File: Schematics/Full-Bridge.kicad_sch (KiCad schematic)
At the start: 3 parts, among them J11 464379202, J12 43650-0418, J13 464369202

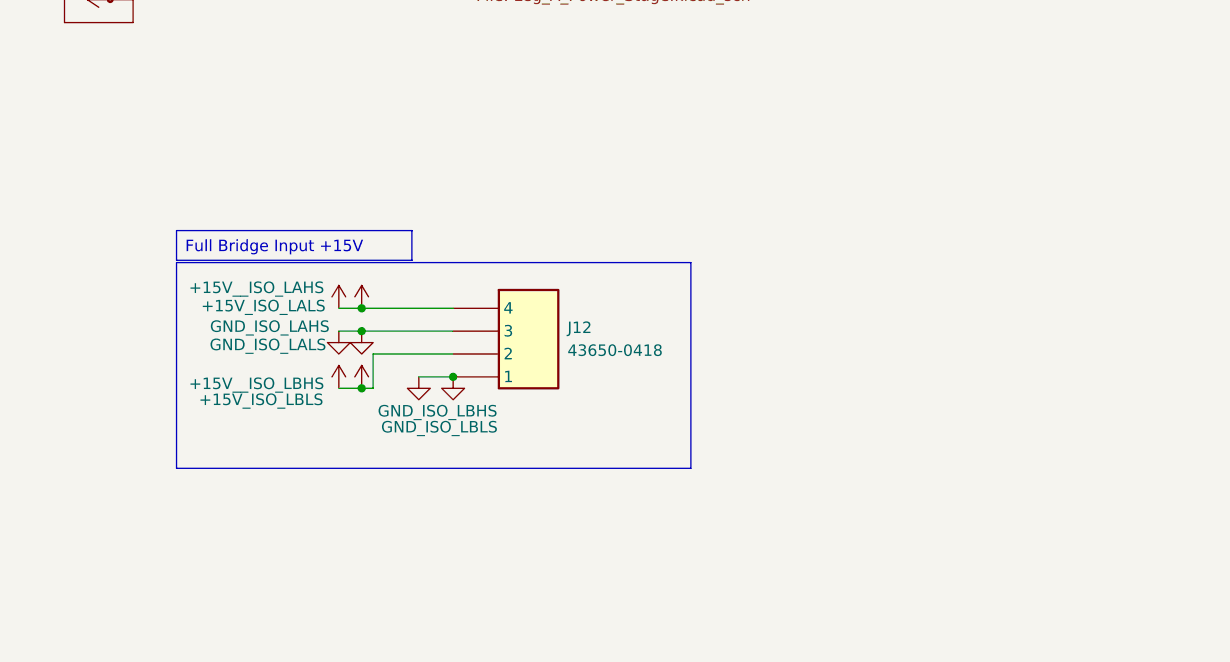
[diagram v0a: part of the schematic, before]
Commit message: [WIP Controller Design]
- Wired up all 64 Pins on the Controller
- Added 3d models for connectors and Controller
- Added data sheets for the newly added parts
- wired connectors to controller to external PCB Boards
- Updated Text fields
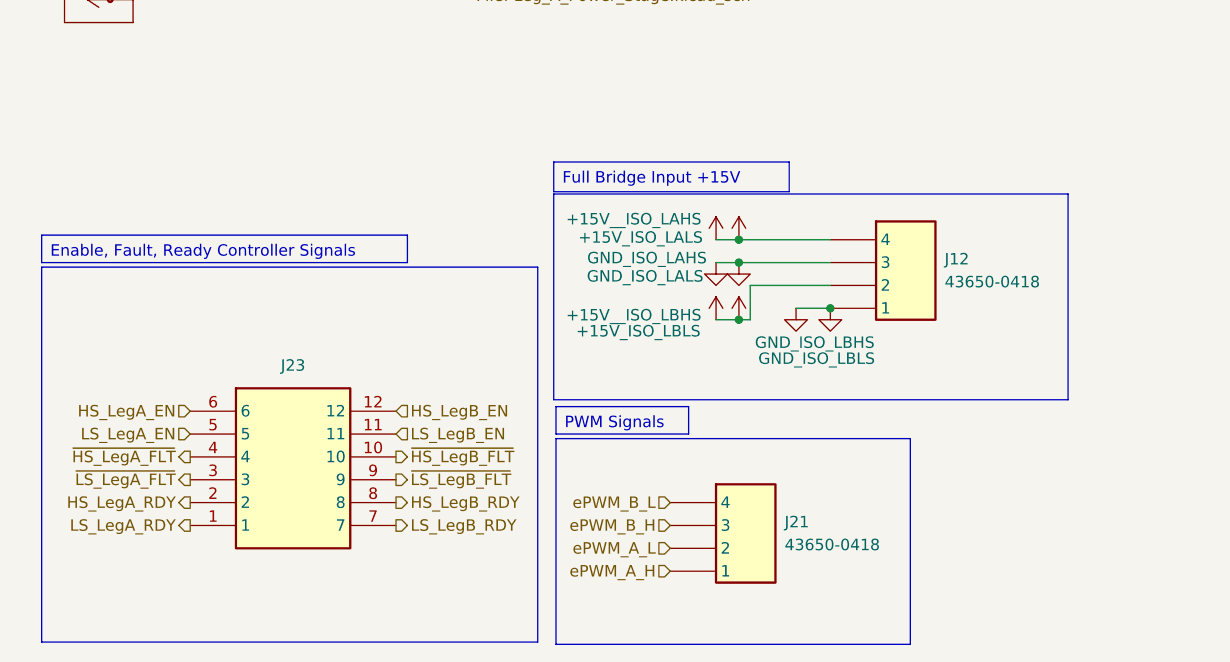
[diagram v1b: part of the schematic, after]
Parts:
- added J21: 43650-0418, SiC_Inverter:436500418, symbol SiC_Inverter:43650-0418
- added J23: 43045-1212, SiC_Inverter:43045-1212, symbol SiC_Inverter:43045-1212
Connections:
- net HS_LegA_EN: now also J23.6
- net HS_LegA_RDY: now also J23.2
- net HS_LegB_EN: now also J23.12
- net HS_LegB_RDY: now also J23.8
- net LS_LegA_EN: now also J23.5
- net LS_LegA_RDY: now also J23.1
- net LS_LegB_EN: now also J23.11
- net LS_LegB_RDY: now also J23.7
- net ~{HS_LegA_FLT}: now also J23.4
- net ~{HS_LegB_FLT}: now also J23.10
- net ~{LS_LegA_FLT}: now also J23.3
- net ~{LS_LegB_FLT}: now also J23.9
- new net ePWM_A_H: J21.1
- new net ePWM_A_L: J21.2
- new net ePWM_B_H: J21.3
- new net ePWM_B_L: J21.4
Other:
- moved on the sheet: J12

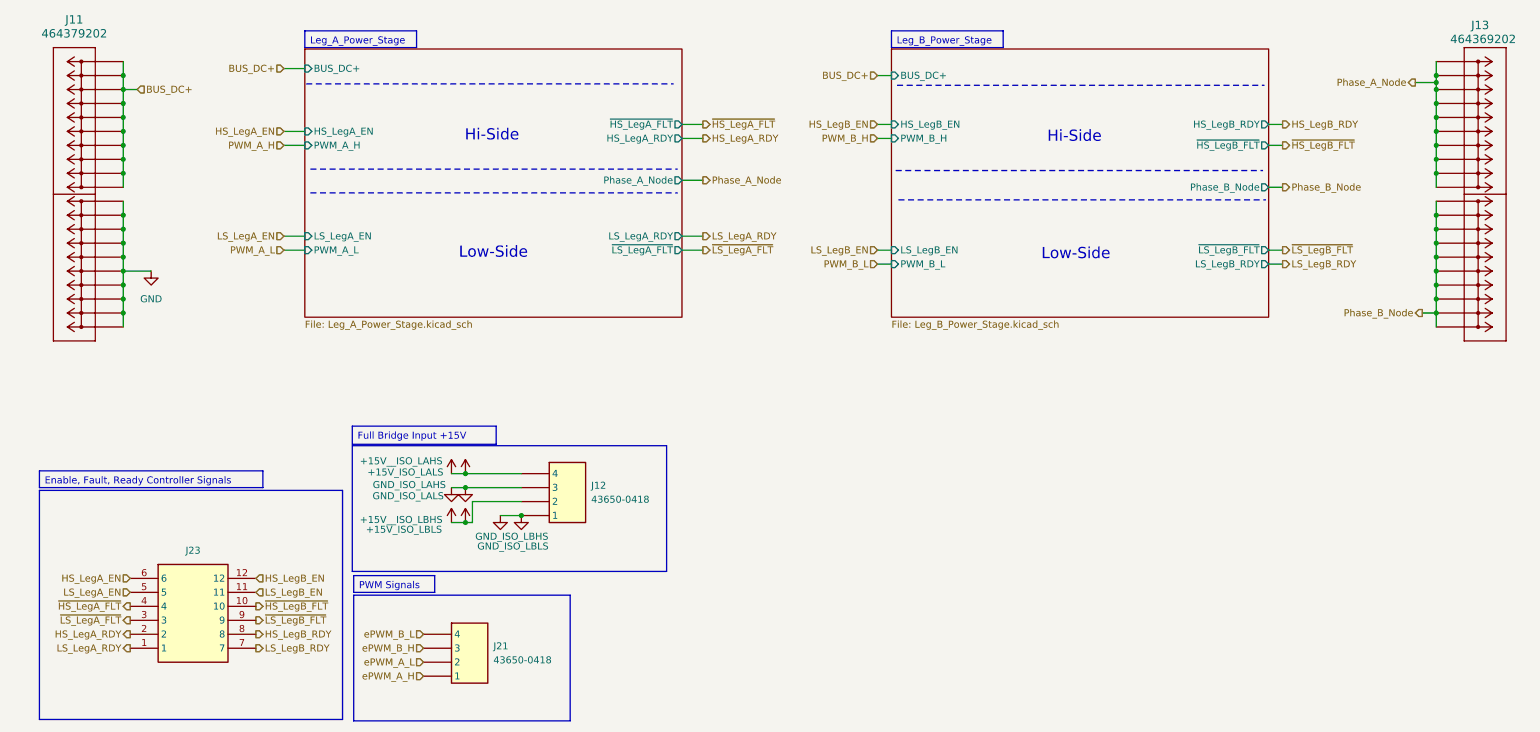
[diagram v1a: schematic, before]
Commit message: [Milestone Compelted Controller and USB]
- Added Test Points
- Completed USB circuit to Controller
- Wired up Controller
- Added Connectors to Power Subsheet and 12pin from cotnroller to Full
  Bridge
- Added 3d models for USB compoents
- General fixes to subsheets
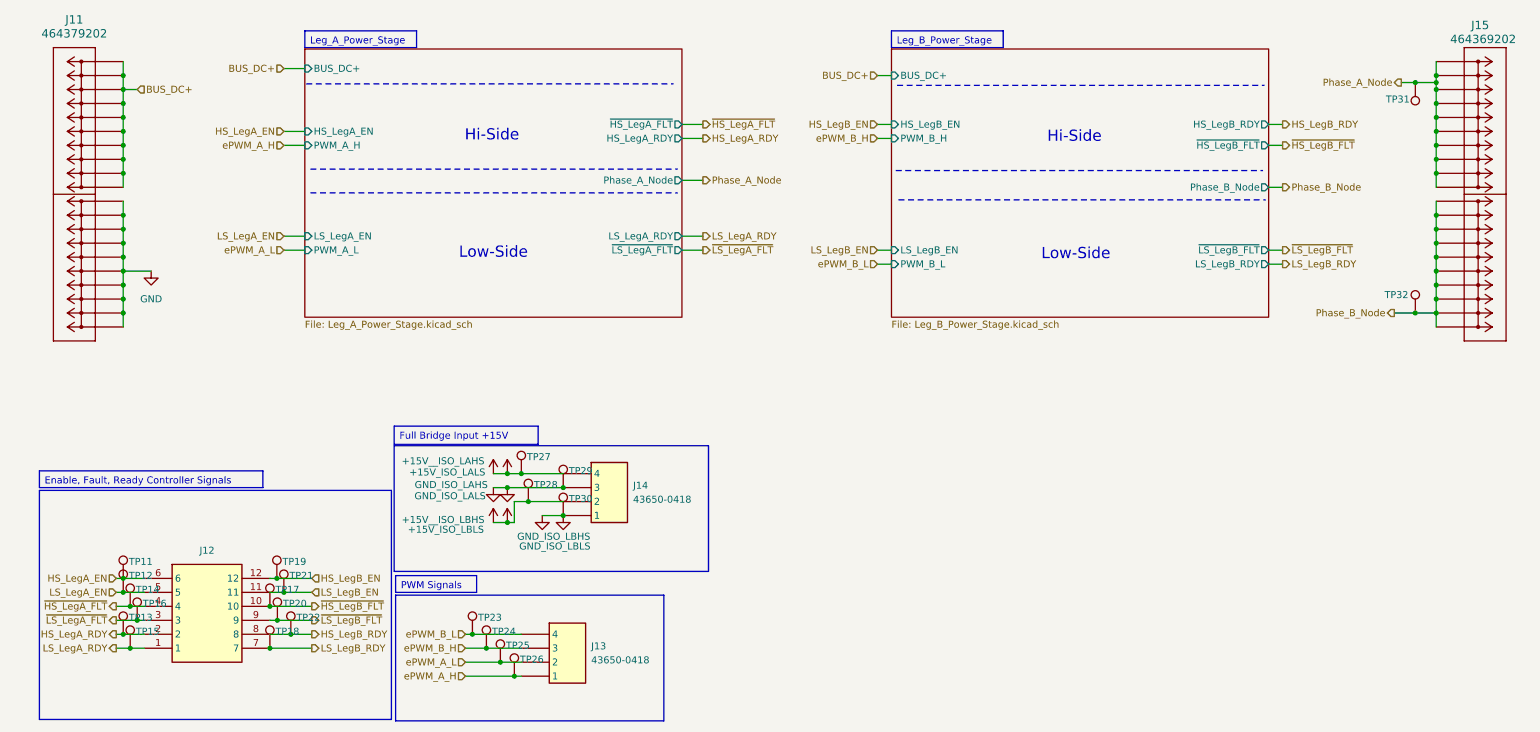
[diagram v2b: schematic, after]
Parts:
- added TP11, TP12, TP13, TP14, TP15, TP16, TP17, TP18, TP19, TP20, TP21, TP22, TP23, TP24, TP25, TP26, TP27, TP28, TP31: 5277, SiC_Inverter:5277, symbol SiC_Inverter:5277
- added TP29, TP30, TP32: 5281, SiC_Inverter:5281, symbol SiC_Inverter:5281
- renumbered J23 to J12, J21 to J13, J12 to J14, J13 to J15
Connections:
- net +15V_ISO_LALS: now also TP27.1
- net +15V_ISO_LBLS: now also TP28.1
- net GND_ISO_LAHS: now also TP29.1
- net GND_ISO_LBHS: now also TP30.1
- net HS_LegA_EN: now also TP11.1
- net HS_LegA_RDY: now also TP13.1
- net HS_LegB_EN: now also TP19.1
- net HS_LegB_RDY: now also TP22.1
- net LS_LegA_EN: now also TP12.1
- net LS_LegA_RDY: now also TP15.1
- net LS_LegB_EN: now also TP21.1
- net LS_LegB_RDY: now also TP18.1
- net Phase_A_Node: now also TP31.1
- net Phase_B_Node: now also TP32.1
- net ePWM_A_H: now also TP26.1
- net ePWM_A_L: now also TP25.1
- net ePWM_B_H: now also TP24.1
- net ePWM_B_L: now also TP23.1
- net ~{HS_LegA_FLT}: now also TP14.1
- net ~{HS_LegB_FLT}: now also TP17.1
- net ~{LS_LegA_FLT}: now also TP16.1
- net ~{LS_LegB_FLT}: now also TP20.1
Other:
- moved on the sheet: J12, J13, J14

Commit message: WIP PCB, Added Test Points, added icon file
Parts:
- renumbered J11 to J12, J12 to J13, J13 to J14, J14 to J15, J15 to J16, TP16 to TP13, TP15 to TP14, TP11 to TP15, TP14 to TP16, TP13 to TP17, TP21 to TP18, TP20 to TP19, TP18 to TP20, TP19 to TP21, TP17 to TP22, TP22 to TP23, TP23 to TP24, TP24 to TP25, TP25 to TP26, TP26 to TP27, TP27 to TP28, TP28 to TP29, TP29 to TP30, TP30 to TP31, TP31 to TP32, TP32 to TP33
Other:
- moved on the sheet: TP12, TP13, TP14, TP15, TP16, TP17, TP18, TP19, TP20, TP21, TP22, TP23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

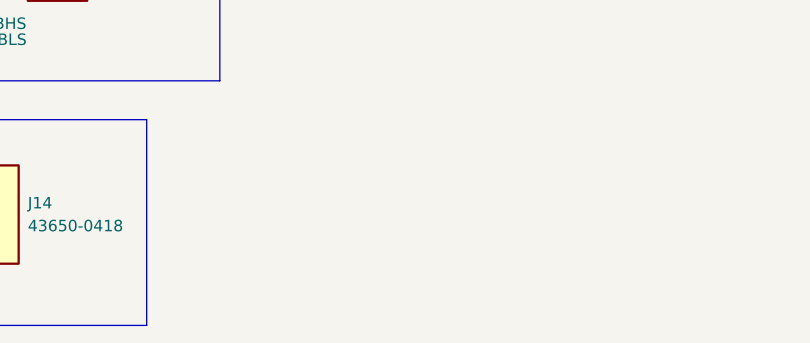
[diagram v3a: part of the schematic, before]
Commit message: Adding Damping Resiter to AC Output Filter and mounting points
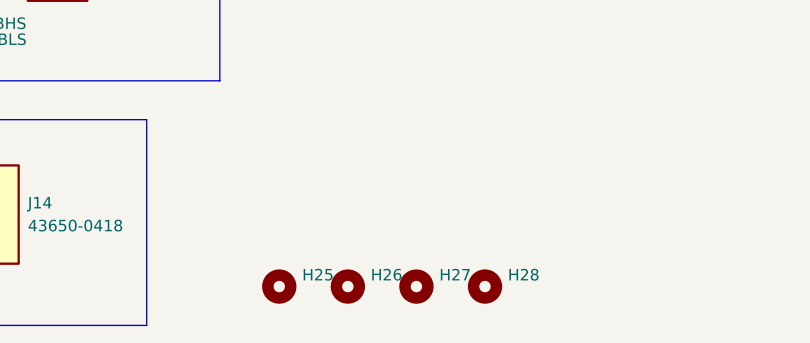
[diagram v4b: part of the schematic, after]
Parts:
- added H25, H26, H27, H28: MountingHole, MountingHole:MountingHole_2.2mm_M2, symbol Mechanical:MountingHole

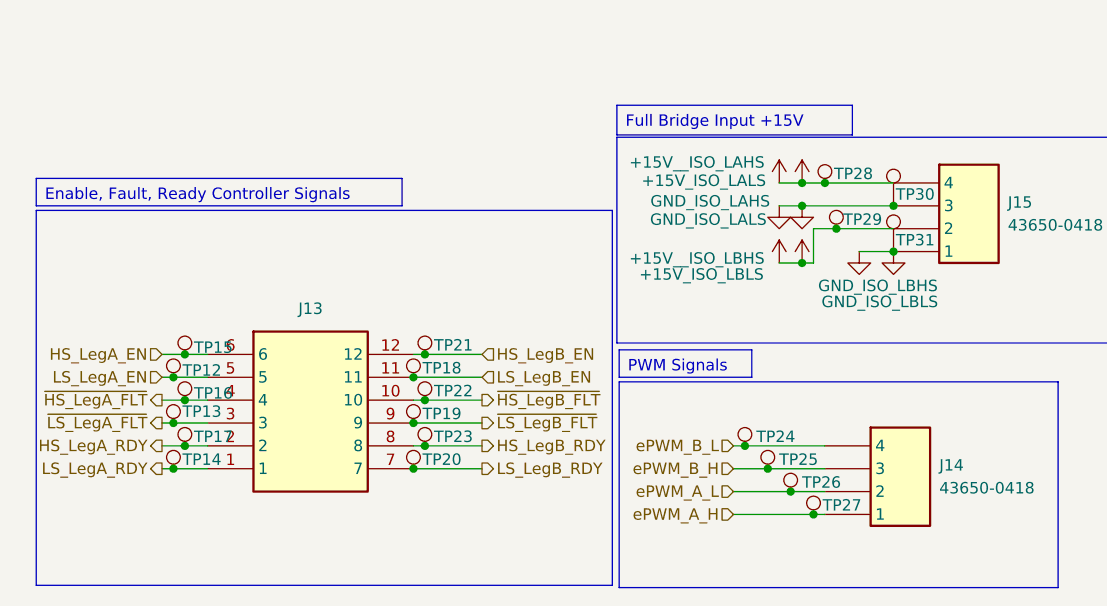
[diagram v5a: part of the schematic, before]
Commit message: Finished Full Bridge Layout
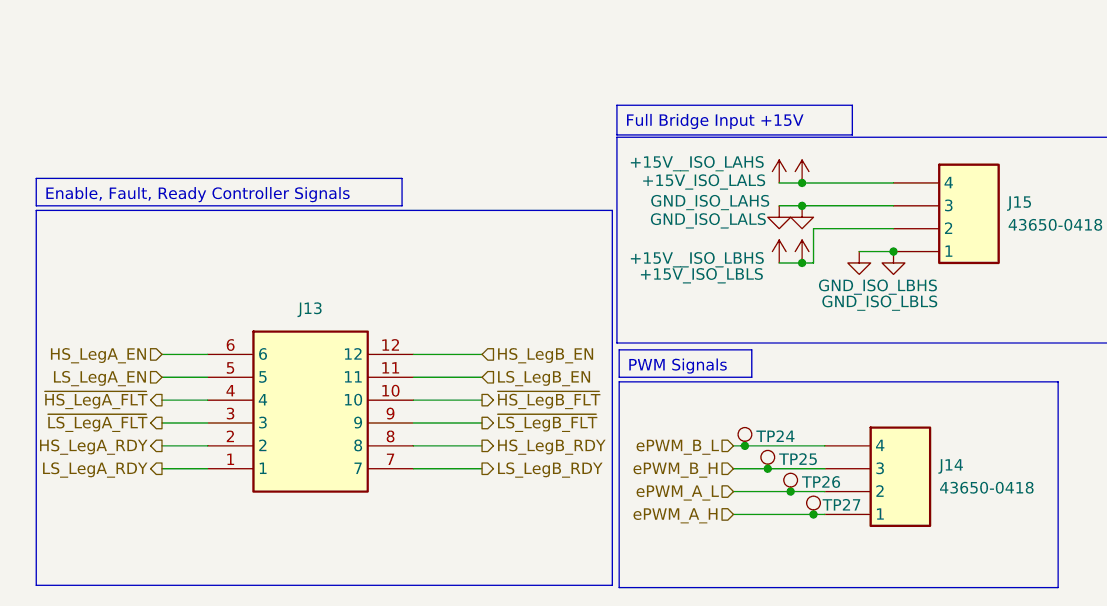
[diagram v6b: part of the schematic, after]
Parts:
- removed TP12, TP13, TP14, TP15, TP16, TP17, TP18, TP19, TP20, TP21, TP22, TP23, TP28, TP29: 5277, SiC_Inverter:5277, symbol SiC_Inverter:5277
- removed TP30, TP31: 5281, SiC_Inverter:5281, symbol SiC_Inverter:5281

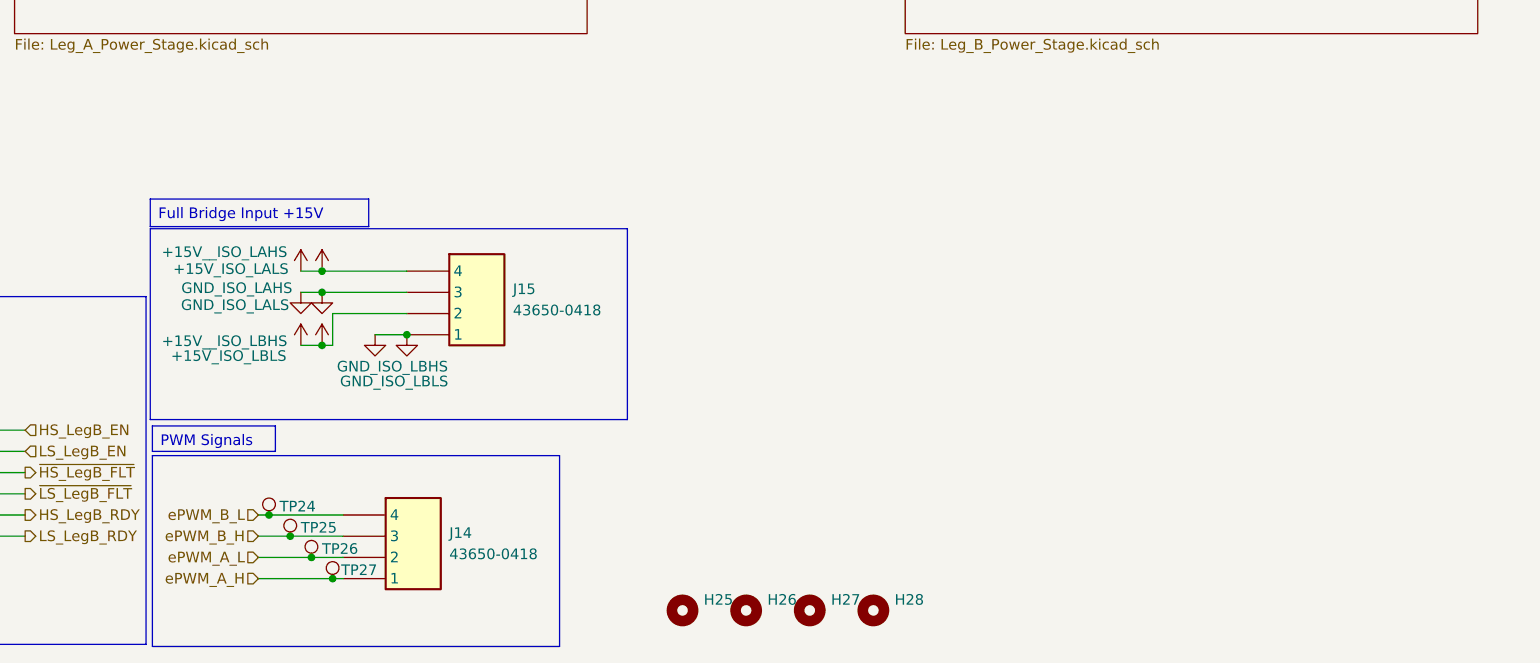
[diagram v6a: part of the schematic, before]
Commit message: Adding two pin connector for 3V3 from power to Full-Bridge
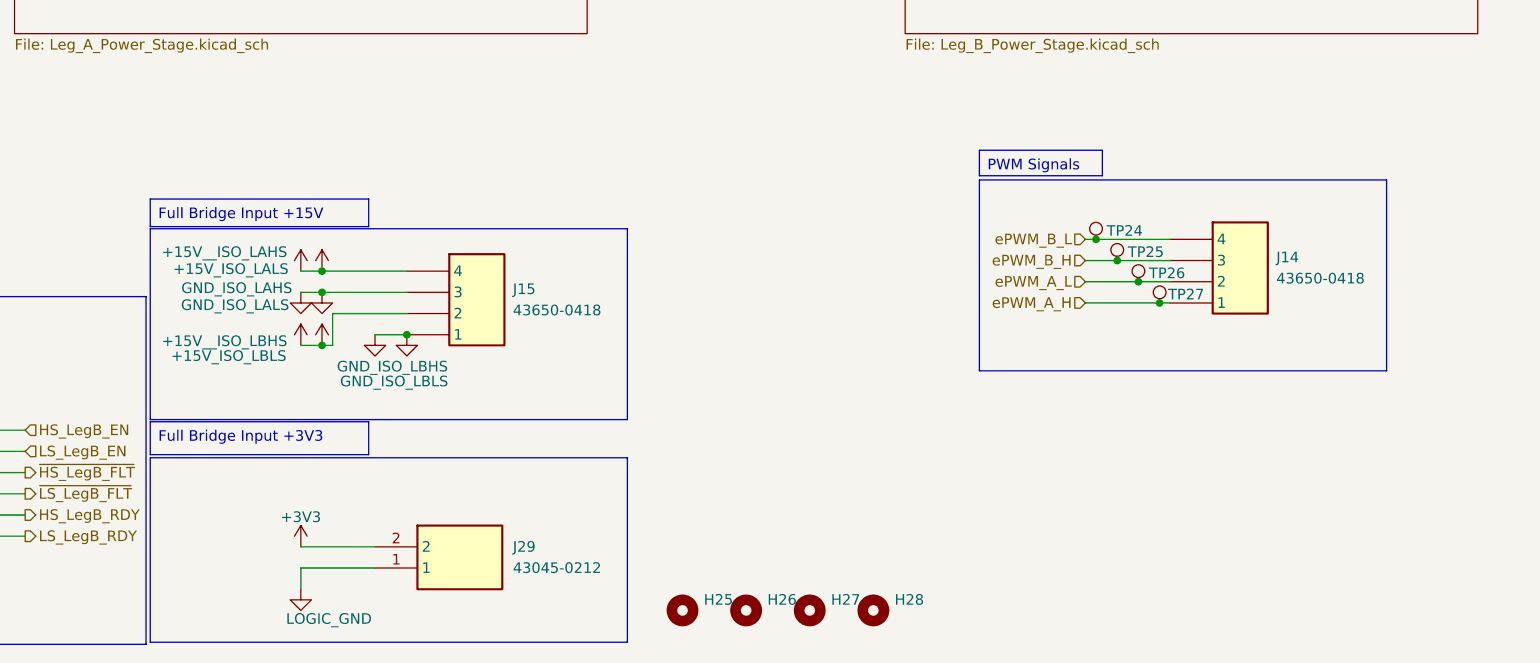
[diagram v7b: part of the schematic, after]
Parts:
- added J29: 43045-0212, 43045-02YY_121314, symbol SiC_Inverter:43045-0212
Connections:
- new net +3V3: J29.2
- new net LOGIC_GND: J29.1
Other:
- moved on the sheet: J14, TP24, TP25, TP26, TP27

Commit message: Added J30 to the Power Board and new Fab output
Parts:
- J29: footprint 43045-02YY_121314 -> SiC_Inverter:43045-0212
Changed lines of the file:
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@@
 			)
 		)
-		(property "Footprint" "43045-02YY_121314"
+		(property "Footprint" "SiC_Inverter:43045-0212"
 			(at 121.92 280.34 0)
 			(hide yes)
